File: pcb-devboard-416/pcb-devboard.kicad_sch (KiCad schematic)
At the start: 28 parts, among them J1 UPDI_PROGRAMMER, J2 PINS1, J3 PINS2, J4 PINS1, J5 PINS1, U1 CH340E, U2 ATtiny412-SS

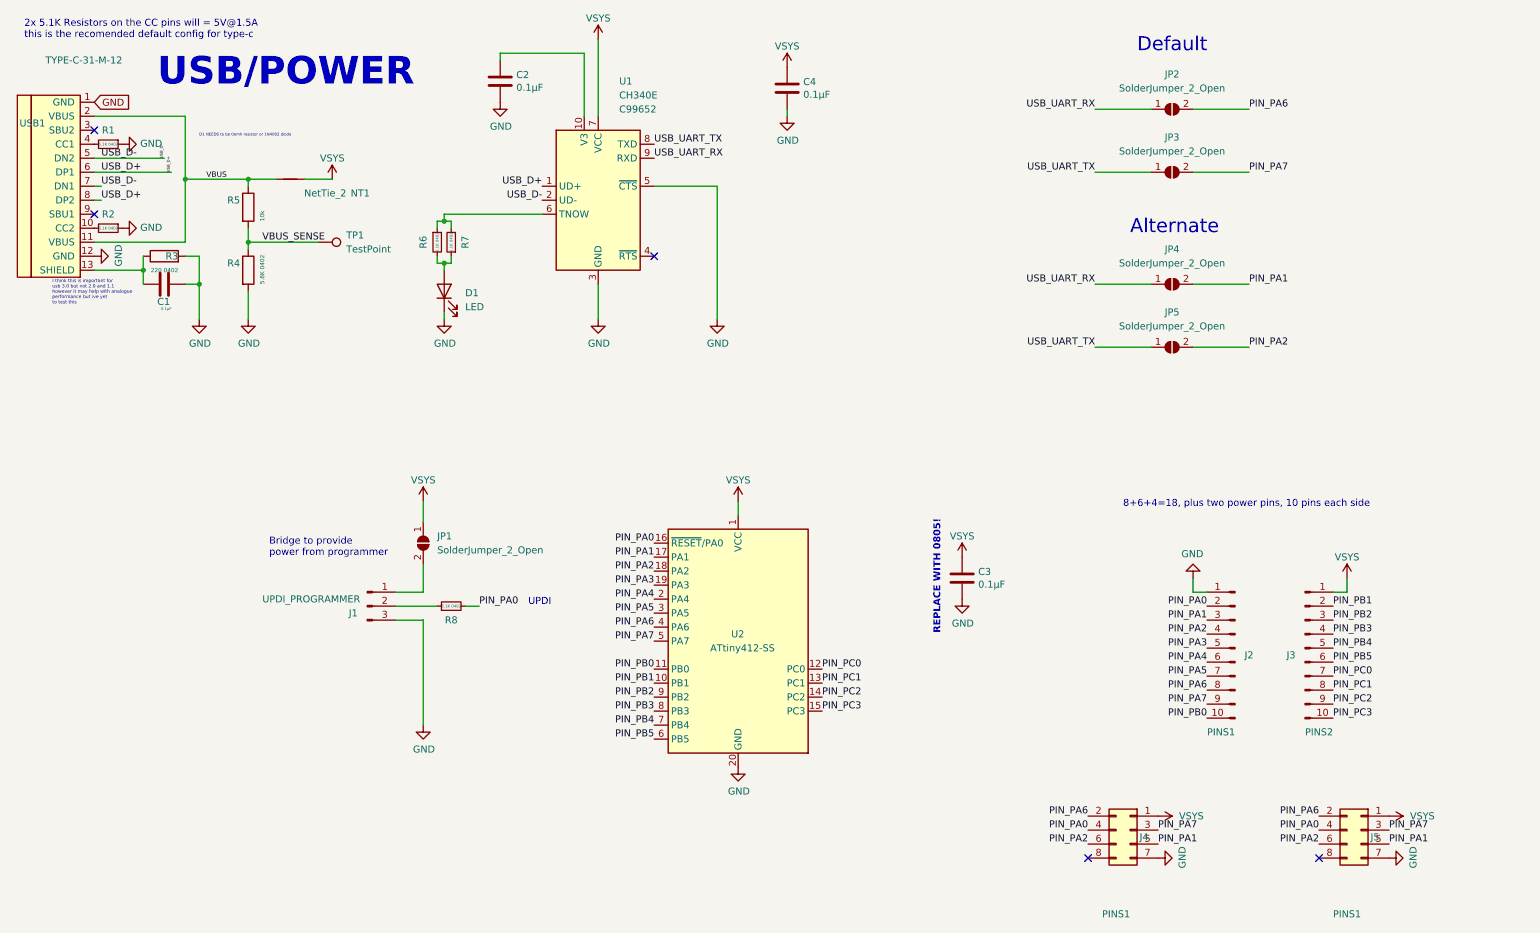
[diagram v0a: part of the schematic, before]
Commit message: 416 dev board: Version 1.0 as manufactured
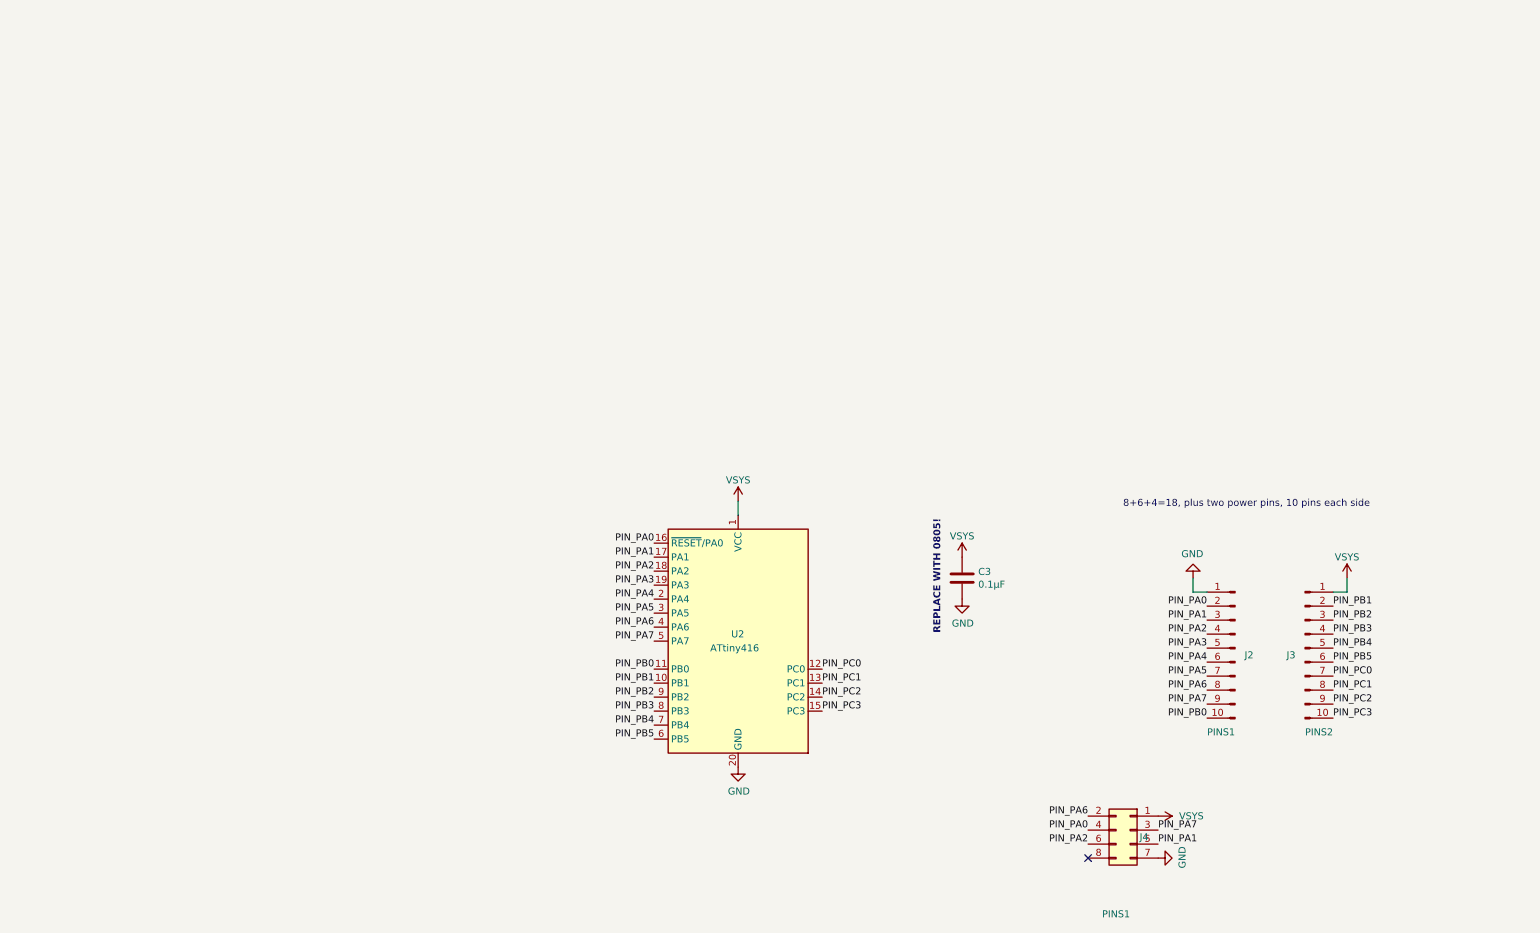
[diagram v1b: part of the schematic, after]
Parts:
- removed C1, C2, C4: 0.1μF, Capacitor_SMD:C_0603_1608Metric, symbol Device:C
- removed D1: LED, LED_SMD:LED_0603_1608Metric, symbol Device:LED
- removed J1: UPDI_PROGRAMMER, Connector_PinHeader_2.54mm:PinHeader_1x03_P2.54mm_Vertical, symbol Connector:Conn_01x03_Male
- removed J5: PINS1, Connector_PinSocket_2.54mm:PinSocket_2x04_P2.54mm_Vertical, symbol Connector_Generic:Conn_02x04_Odd_Even
- removed JP1, JP2, JP3, JP4, JP5: SolderJumper_2_Open, Jumper:SolderJumper-2_P1.3mm_Open_Pad1.0x1.5mm, symbol Jumper:SolderJumper_2_Open
- removed NT1: NetTie_2, NetTie:NetTie-2_SMD_Pad0.5mm, symbol Device:NetTie_2
- removed R1, R2, R6, R7, R8: 5.1K 0402, Resistor_SMD:R_0402_1005Metric, symbol Device:R_Small
- removed R3: 220 0402, Resistor_SMD:R_0402_1005Metric, symbol Device:R
- removed R4: 5.6K 0402, Resistor_SMD:R_0402_1005Metric, symbol Device:R
- removed R5: 10k, Resistor_SMD:R_0402_1005Metric, symbol Device:R
- removed TP1: TestPoint, mine:TestPoint_Pad_1.0x1.0mm, symbol Connector:TestPoint
- removed U1: CH340E, Package_SO:MSOP-10_3x3mm_P0.5mm, symbol _my_kicad_library:CH340E
- removed USB1: TYPE-C-31-M-12, HRO:HRO-TYPE-C-31-M-12, symbol Type-C:HRO-TYPE-C-31-M-12
- C3: footprint Capacitor_SMD:C_0603_1608Metric -> mine:my_C_0805_2012Metric_Pad1.15x1.40mm_HandSolder
- U2: value ATtiny412-SS -> ATtiny416
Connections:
- no-connect marks 5 -> 1
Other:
- note removed: "2x 5.1K Resistors on the CC pins will = 5V@1.5A this is the recomended default config for type-c"
- note removed: "Alternate"
- note removed: "Bridge to provide power from programmer"
- note removed: "D1 NEEDS to be 0omh resistor or 1N4002 diode"
- note removed: "Default"
- note removed: "I think this is important for usb 3.0 but not 2.0 and 1.1 however it may help with analogue performance but ive yet to test this"
- note removed: "UPDI"
- note removed: "USB/POWER"

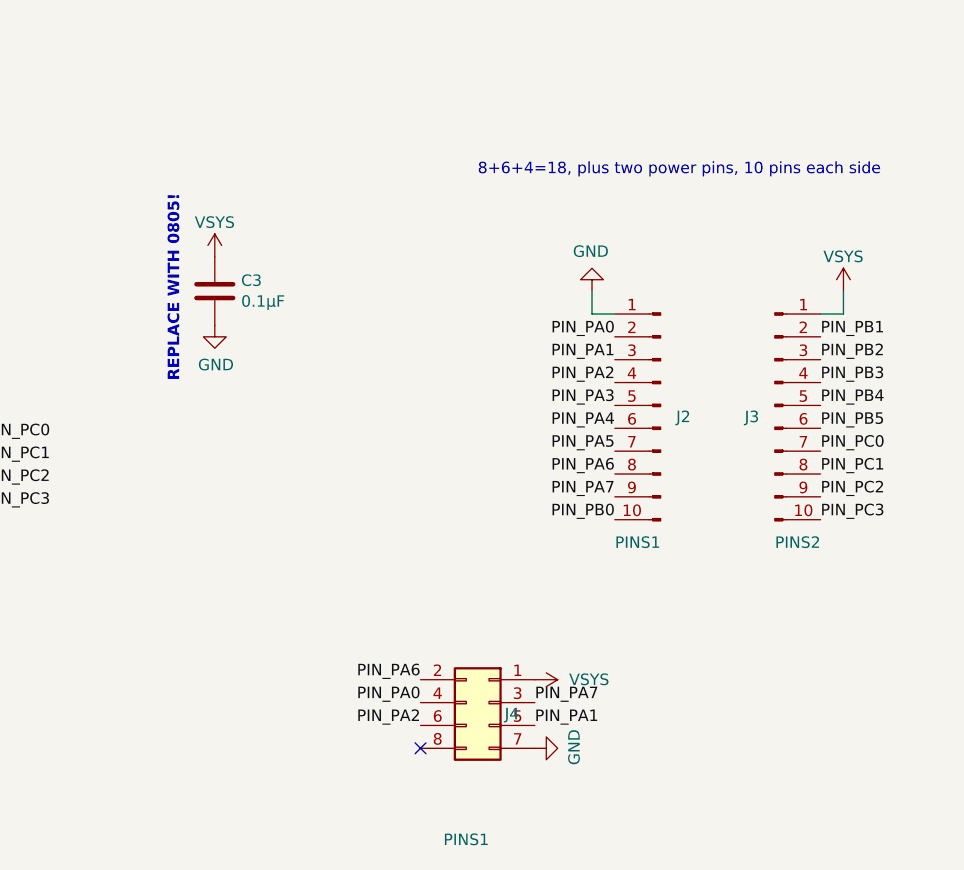
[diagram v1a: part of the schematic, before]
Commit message: 41x interface board: Version 1.1 as manufactured
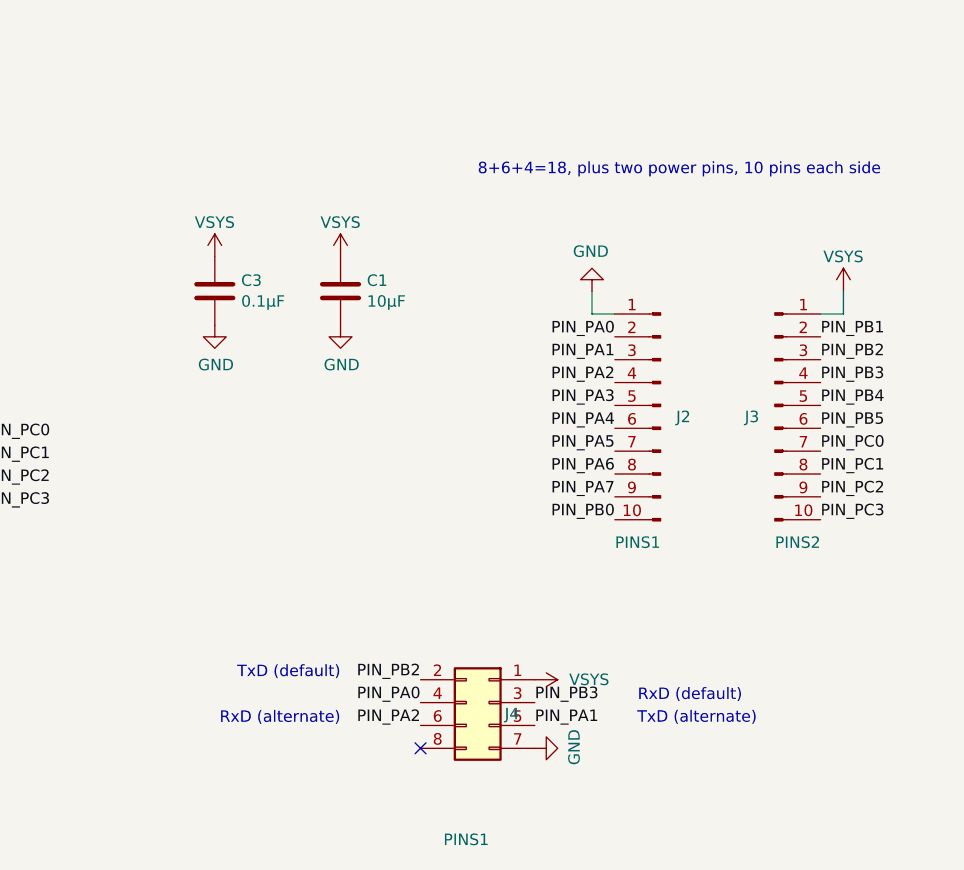
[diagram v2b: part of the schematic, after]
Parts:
- added C1: 10μF, mine:my_C_0805_2012Metric_Pad1.15x1.40mm_HandSolder, symbol Device:C
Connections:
- net GND: now also C1.2
- net PIN_PA6: no longer J4.2 (Pin_2)
- net PIN_PA7: no longer J4.3 (Pin_3)
- net PIN_PB2: now also J4.2 (Pin_2)
- net PIN_PB3: now also J4.3 (Pin_3)
- net VSYS: now also C1.1
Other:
- note added: "RxD (alternate)"
- note added: "RxD (default)"
- note added: "TxD (alternate)"
- note added: "TxD (default)"
- note removed: "REPLACE WITH 0805!"
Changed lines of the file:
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@@
     (stroke (width 0) (type default) (color 0 0 0 0))
   )
+  (text "TxD (alternate)" (at 233.6352 165.0879 0)
+    (effects (font (size 1.27 1.27)) (justify left bottom))
+  )
   (text "8+6+4=18, plus two power pins, 10 pins each side" (at 215.9 104.14 0)
     (effects (font (size 1.27 1.27)) (justify left bottom))
   )
-  (text "REPLACE WITH 0805!" (at 182.88 127 90)
-    (effects (font (size 1.27 1.27) (thickness 0.254) bold) (justify left bottom))
+  (text "RxD (default)" (at 233.68 162.56 0)
+    (effects (font (size 1.27 1.27)) (justify left bottom))
+  )
+  (text "TxD (default)" (at 200.66 160.02 180)
+    (effects (font (size 1.27 1.27)) (justify right bottom))
+  )
+  (text "RxD (alternate)" (at 200.66 165.1 180)
+    (effects (font (size 1.27 1.27)) (justify right bottom))
   )
   (label "PIN_PB5" (at 130.81 146.05 180)
@@
     (effects (font (size 1.27 1.27)) (justify left bottom))
   )
-  (label "PIN_PA7" (at 222.25 162.56 0)
+  (label "PIN_PB3" (at 222.25 162.56 0)
     (effects (font (size 1.27 1.27)) (justify left bottom))
   )
@@
     (effects (font (size 1.27 1.27)) (justify right bottom))
   )
-  (label "PIN_PA6" (at 209.55 160.02 180)
+  (label "PIN_PB2" (at 209.55 160.02 180)
     (effects (font (size 1.27 1.27)) (justify right bottom))
   )
@@
     )
     (property "Datasheet" "" (id 3) (at 186.69 113.03 0)
+      (effects (font (size 1.27 1.27)) hide)
+    )
+    (pin "1")
+  )
+  (symbol (lib_id "power:GND") (at 200.66 120.65 0) (unit 1)
+    (in_bom yes) (on_board yes)
+    (property "Reference" "#PWR02" (id 0) (at 200.66 127 0)
+      (effects (font (size 1.27 1.27)) hide)
+    )
+    (property "Value" "GND" (id 1) (at 200.787 125.0442 0))
+    (property "Footprint" "" (id 2) (at 200.66 120.65 0)
+      (effects (font (size 1.27 1.27)) hide)
+    )
+    (property "Datasheet" "" (id 3) (at 200.66 120.65 0)
       (effects (font (size 1.27 1.27)) hide)
     )
@@
     (pin "1")
   )
+  (symbol (lib_id "Device:C") (at 200.66 116.84 0) (unit 1)
+    (in_bom yes) (on_board yes)
+    (property "Reference" "C1" (id 0) (at 203.581 115.6716 0)
+      (effects (font (size 1.27 1.27)) (justify left))
+    )
+    (property "Value" "10μF" (id 1) (at 203.581 117.983 0)
+      (effects (font (size 1.27 1.27)) (justify left))
+    )
+    (property "Footprint" "mine:my_C_0805_2012Metric_Pad1.15x1.40mm_HandSolder" (id 2) (at 201.6252 120.65 0)
+      (effects (font (size 1.27 1.27)) hide)
+    )
+    (property "Datasheet" "~" (id 3) (at 200.66 116.84 0)
+      (effects (font (size 1.27 1.27)) hide)
+    )
+    (property "LCSC" "C14663" (id 4) (at 200.66 116.84 0)
+      (effects (font (size 1.27 1.27)) hide)
+    )
+    (pin "1")
+    (pin "2")
+  )
   (symbol (lib_id "Connector_Generic:Conn_02x04_Odd_Even") (at 217.17 162.56 0) (mirror y) (unit 1)
     (in_bom yes) (on_board yes)
@@
     )
     (property "Datasheet" "" (id 3) (at 256.54 116.84 0)
+      (effects (font (size 1.27 1.27)) hide)
+    )
+    (pin "1")
+  )
+  (symbol (lib_id "_my_kicad_library:VSYS") (at 200.66 113.03 0) (unit 1)
+    (in_bom yes) (on_board yes) (fields_autoplaced)
+    (property "Reference" "#PWR01" (id 0) (at 200.66 116.84 0)
+      (effects (font (size 1.27 1.27)) hide)
+    )
+    (property "Value" "VSYS" (id 1) (at 200.66 109.22 0))
+    (property "Footprint" "" (id 2) (at 200.66 113.03 0)
+      (effects (font (size 1.27 1.27)) hide)
+    )
+    (property "Datasheet" "" (id 3) (at 200.66 113.03 0)
       (effects (font (size 1.27 1.27)) hide)
     )
@@
       (reference "#FLG02") (unit 1) (value "PWR_FLAG") (footprint "")
     )
+    (path "/c4b48812-745a-4422-a720-60fb726634f7"
+      (reference "#PWR01") (unit 1) (value "VSYS") (footprint "")
+    )
+    (path "/0dcaf8e6-6256-4a75-9348-d18d71028b3e"
+      (reference "#PWR02") (unit 1) (value "GND") (footprint "")
+    )
     (path "/4e3216cc-91d9-4120-bc5e-bc6736d90aa7"
       (reference "#PWR014") (unit 1) (value "VSYS") (footprint "")
@@
       (reference "#PWR0102") (unit 1) (value "VSYS") (footprint "")
     )
+    (path "/4b005d71-3849-4217-93db-419ba7f5e87f"
+      (reference "C1") (unit 1) (value "10μF") (footprint "mine:my_C_0805_2012Metric_Pad1.15x1.40mm_HandSolder")
+    )
     (path "/fdd5b696-4e43-46fd-a0e8-bfe3c1fbb292"
